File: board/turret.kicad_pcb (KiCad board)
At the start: 2 copper layers, 29 parts, among them M1 SRV_LAS, M2 SRV_SEN, U1 STM32F103CBTx, U2 W25Q32JVSS, U3 TPA2005D1DGN

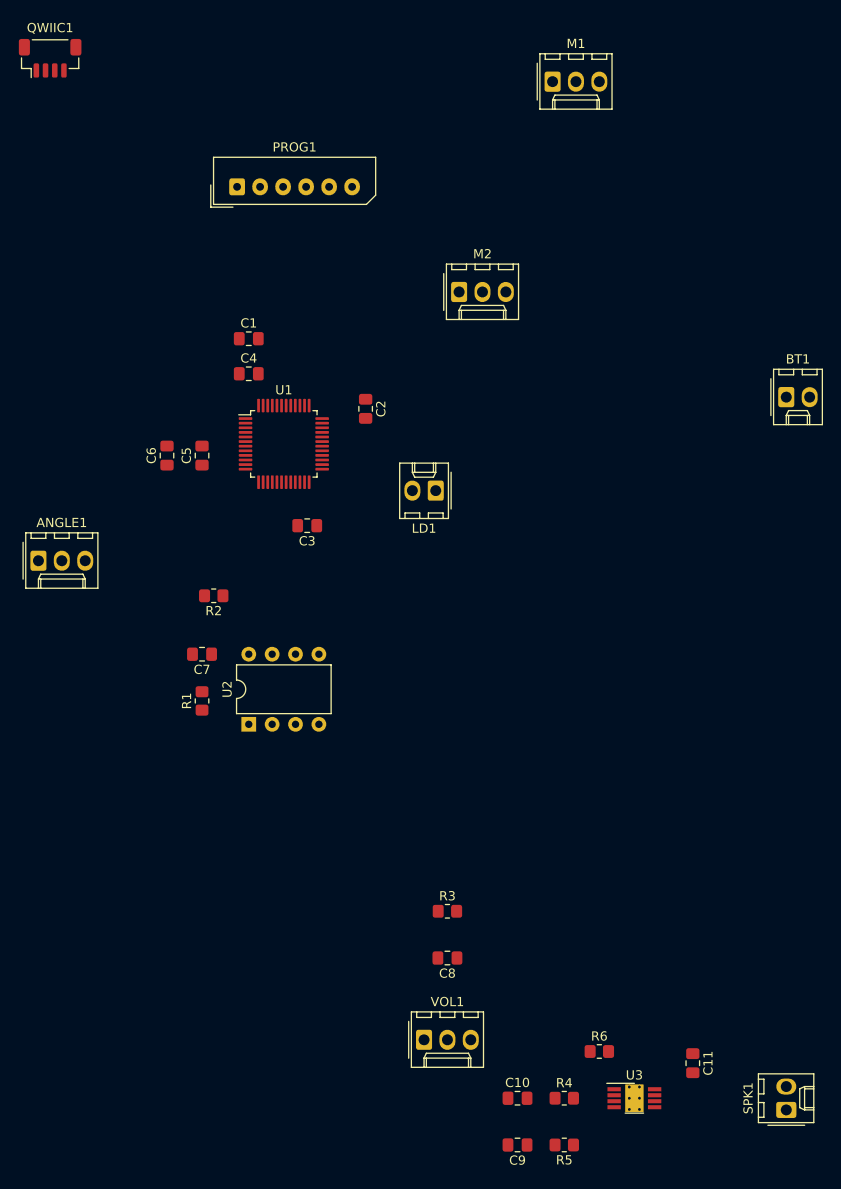
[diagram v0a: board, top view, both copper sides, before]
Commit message: Partially route board
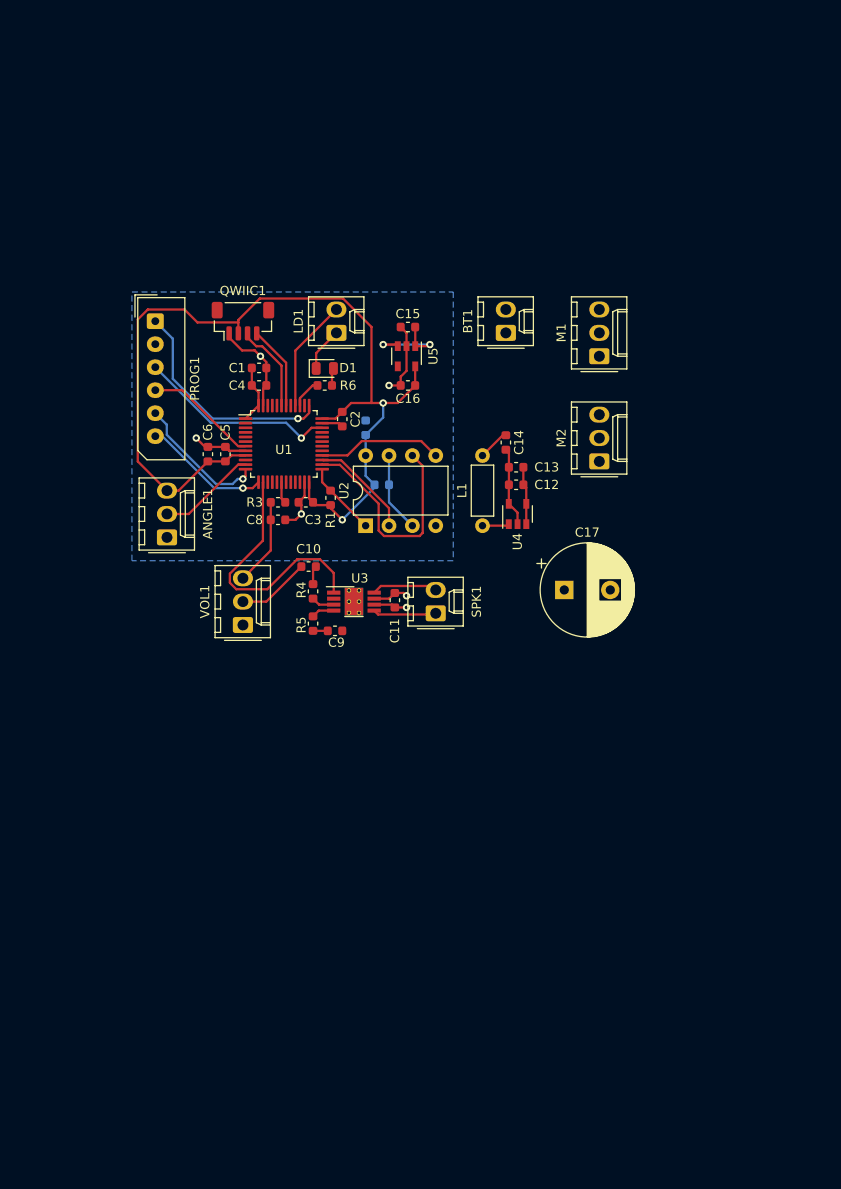
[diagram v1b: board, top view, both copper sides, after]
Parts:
- added C12: 22u, Capacitor_SMD:C_0603_1608Metric, F.Cu at (91.3, 69.2)
- added C13: 22u, Capacitor_SMD:C_0603_1608Metric, F.Cu at (91.3, 67.3)
- added C14: 4u7, Capacitor_SMD:C_0603_1608Metric, F.Cu at (90.2, 64.6)
- added C15: 100n, Capacitor_SMD:C_0603_1608Metric, F.Cu at (79.5, 52.1)
- added C16: 100n, Capacitor_SMD:C_0603_1608Metric, F.Cu at (79.5, 58.4)
- added C17: 1000u, Capacitor_THT:CP_Radial_D10.0mm_P5.00mm, F.Cu at (96.5, 80.6)
- added D1: LED, LED_SMD:LED_0805_2012Metric, F.Cu at (70.5, 56.6)
- added L1: 2u2, Inductor_THT:L_Axial_L5.3mm_D2.2mm_P7.62mm_Horizontal_Vishay_IM-1, F.Cu at (87.6, 73.7)
- added U4: TPS61322xADBV, Package_TO_SOT_SMD:SOT-23-5, F.Cu at (91.4, 72.4)
- added U5: TLV70028_SOT23-5, Package_TO_SOT_SMD:SOT-23-5, F.Cu at (79.4, 55.2)
- C1, C10, C11, C2, C3, C4, C5, C6, C8, C9: footprint Capacitor_SMD:C_0805_2012Metric_Pad1.18x1.45mm_HandSolder -> Capacitor_SMD:C_0603_1608Metric
- C7: footprint Capacitor_SMD:C_0805_2012Metric_Pad1.18x1.45mm_HandSolder -> Capacitor_SMD:C_0603_1608Metric; moved to B.Cu
- R1, R4, R5: footprint Resistor_SMD:R_0805_2012Metric_Pad1.20x1.40mm_HandSolder -> Resistor_SMD:R_0603_1608Metric
- R2: footprint Resistor_SMD:R_0805_2012Metric_Pad1.20x1.40mm_HandSolder -> Resistor_SMD:R_0603_1608Metric; moved to B.Cu
- R3: value 400 -> 200; footprint Resistor_SMD:R_0805_2012Metric_Pad1.20x1.40mm_HandSolder -> Resistor_SMD:R_0603_1608Metric
- R6: value 50K -> 100; footprint Resistor_SMD:R_0805_2012Metric_Pad1.20x1.40mm_HandSolder -> Resistor_SMD:R_0603_1608Metric
- moved R6 78.3 mm to (70.5, 58.4), turned to 180 degrees
- moved SPK1 66.1 mm to (82.5, 83.2)
- moved R5 62.9 mm to (69.2, 84.3), turned to 270 degrees
- moved C10 62.1 mm to (68.7, 78.1)
- moved U3 62.0 mm to (73.7, 81.9)
- moved R4 61.5 mm to (69.2, 80.8), turned to 270 degrees
- moved C11 59.8 mm to (78.1, 81.8)
- moved C9 59.3 mm to (71.6, 85.1), turned to 0 degrees
- moved C8 51.1 mm to (65.4, 73.0), turned to 0 degrees
- moved VOL1 49.2 mm to (61.6, 84.5), turned to 90 degrees
- moved R3 48.1 mm to (65.4, 71.1), turned to 180 degrees
- moved QWIIC1 35.4 mm to (61.6, 51.4)
- moved BT1 31.3 mm to (90.2, 52.7), turned to 90 degrees
- moved C7 30.4 mm to (74.9, 63.0), turned to 90 degrees
- moved M1 30.3 mm to (100.3, 55.2), turned to 90 degrees
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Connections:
- ANGLE1 pad 3: +3V3 -> VDD
- BT1 pad 1: +3V3 -> Net-(BT1-Pad1)
- BT1 pad 2: (no net) -> GNDA
- C1 pad 1: +3V3 -> VDD
- C11 pad 2: +3V3 -> +5V
- C2 pad 1: +3V3 -> VDD
- C3 pad 1: +3V3 -> VDD
- C4 pad 1: +3V3 -> VDD
- C5 pad 1: +3V3 -> VDD
- C6 pad 1: +3V3 -> VDD
- C7 pad 1: +3V3 -> VDD
- M1 pad 2: +3V3 -> +5V
- M2 pad 2: +3V3 -> +5V
- QWIIC1 pad 2: +3V3 -> VDD
- R1 pad 2: +3V3 -> VDD
- R2 pad 2: +3V3 -> VDD
- R6 pad 1: /MUTE -> Net-(D1-Pad2)
- R6 pad 2: Net-(R6-Pad2) -> /TGT_LED
- U1 pad 1: +3V3 -> VDD
- U1 pad 10: (no net) -> Net-(U1-Pad10)
- U1 pad 14: /SPI_NSS -> /AU_ENAB
- U1 pad 15: /SPI_SCK -> Net-(U1-Pad15)
- U1 pad 16: /SPI_MISO -> Net-(U1-Pad16)
- U1 pad 17: /SPI_MOSI -> Net-(U1-Pad17)
- U1 pad 18: (no net) -> /AUDIO
- U1 pad 19: (no net) -> Net-(U1-Pad19)
- U1 pad 2: (no net) -> Net-(U1-Pad2)
- U1 pad 20: (no net) -> Net-(U1-Pad20)
- U1 pad 21: (no net) -> Net-(U1-Pad21)
- U1 pad 22: (no net) -> Net-(U1-Pad22)
- U1 pad 24: +3V3 -> VDD
- U1 pad 25: (no net) -> /SPI_NSS
- U1 pad 26: (no net) -> /SPI_SCK
- U1 pad 27: /LASER -> /SPI_MISO
- U1 pad 28: (no net) -> /SPI_MOSI
- U1 pad 29: /AUDIO -> /SRV_SEN
- U1 pad 3: (no net) -> Net-(U1-Pad3)
- U1 pad 30: /MUTE -> /SRV_LAS
- U1 pad 31: (no net) -> Net-(U1-Pad31)
- U1 pad 32: (no net) -> Net-(U1-Pad32)
- U1 pad 33: (no net) -> Net-(U1-Pad33)
- U1 pad 36: +3V3 -> VDD
- U1 pad 38: (no net) -> Net-(U1-Pad38)
- U1 pad 39: (no net) -> /TGT_LED
- U1 pad 4: (no net) -> Net-(U1-Pad4)
- U1 pad 40: /SRV_SEN -> /LASER
- U1 pad 41: /SRV_LAS -> Net-(U1-Pad41)
- U1 pad 44: (no net) -> Net-(U1-Pad44)
- U1 pad 45: (no net) -> Net-(U1-Pad45)
- U1 pad 46: (no net) -> Net-(U1-Pad46)
- U1 pad 48: +3V3 -> VDD
- U1 pad 5: (no net) -> Net-(U1-Pad5)
- U1 pad 6: (no net) -> Net-(U1-Pad6)
- U1 pad 9: +3V3 -> VDD
- U2 pad 8: +3V3 -> VDD
- U3 pad 1: Net-(R6-Pad2) -> /AU_ENAB
- U3 pad 6: +3V3 -> +5V
- U3 pad 9: (no net) -> GNDA
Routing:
- net VDD: track 0.00 -> 110.4 mm, vias 0 -> 2
- net GNDA: track 0.00 -> 50.0 mm, vias 0 -> 5
- net /AU_ENAB: track 0.00 -> 28.1 mm
- net /SPI_SCK: track 0.00 -> 24.9 mm
- net /SWCLK: track 0.00 -> 24.7 mm, vias 0 -> 1
- net /SWDIO: track 0.00 -> 21.8 mm, vias 0 -> 1
- net /SER_TX: track 0.00 -> 14.8 mm, vias 0 -> 1
- net Net-(BT1-Pad1): track 0.00 -> 13.9 mm, vias 0 -> 2
- net /SER_RX: track 0.00 -> 13.8 mm, vias 0 -> 1
- net /SPI_MOSI: track 0.00 -> 13.6 mm
- net /RESET: track 0.00 -> 12.3 mm
- net /LASER: track 0.00 -> 12.3 mm
- net /SPI_MISO: track 0.00 -> 11.3 mm
- net /ANGLE_POT: track 0.00 -> 10.8 mm
- net +5V: track 0.00 -> 9.95 mm, vias 0 -> 1
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- added copper zone on B.Cu, net GNDA

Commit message: Route PCB
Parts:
- added C18: 100p, Capacitor_SMD:C_0603_1608Metric, F.Cu at (91.9, 77.5)
- added C19: 20p, Capacitor_SMD:C_0603_1608Metric, F.Cu at (91.9, 79.4)
- added D2: D_Schottky, Diode_SMD:D_SMA, F.Cu at (90.1, 74.9)
- added Q1: BC547, Package_TO_SOT_THT:TO-92_Inline_Wide, F.Cu at (97.2, 82.5)
- added R7: 5, Resistor_SMD:R_0603_1608Metric, F.Cu at (88.5, 77.5)
- added R8: 1K, Resistor_SMD:R_0603_1608Metric, F.Cu at (87.4, 82.5)
- L1: footprint Inductor_THT:L_Axial_L5.3mm_D2.2mm_P7.62mm_Horizontal_Vishay_IM-1 -> Inductor_THT:L_Axial_L7.0mm_D3.3mm_P10.16mm_Horizontal_Fastron_MICC
- R6: value 100 -> 50
- moved LD1 40.5 mm to (102.2, 79.4)
- moved C17 24.7 mm to (91.4, 56.5), turned to 90 degrees
- moved M1 17.3 mm to (102.2, 72.4)
- moved BT1 12.1 mm to (102.2, 53.3)
- moved C9 10.3 mm to (61.4, 83.2), turned to 180 degrees
- moved VOL1 9.86 mm to (52.1, 81.9), turned to 0 degrees
- moved C10 7.72 mm to (61.4, 80.6)
- moved R2 5.17 mm to (77.6, 64.1)
- moved R5 4.73 mm to (64.6, 83.2), turned to 180 degrees
- moved R4 4.60 mm to (64.6, 80.6), turned to 0 degrees
- moved M2 4.26 mm to (102.2, 62.9)
- moved C11 3.81 mm to (74.3, 81.8)
- moved SPK1 3.81 mm to (78.7, 83.2)
- moved U3 3.81 mm to (69.8, 81.9)
- moved C12 2.29 mm to (92.6, 67.3)
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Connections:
- C17 pad 1: +5V -> Net-(BT1-Pad1)
- LD1 pad 1: GNDA -> Net-(LD1-Pad1)
- LD1 pad 2: /LASER -> +5V
- U1 pad 15: Net-(U1-Pad15) -> /LASER
- U1 pad 40: /LASER -> Net-(U1-Pad40)
- U3 pad 2: (no net) -> Net-(U3-Pad2)
- U5 pad 4: Net-(U5-Pad4) -> GNDA
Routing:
- net /SRV_LAS: track 0.00 -> 69.0 mm
- net +5V: track 9.95 -> 78.8 mm, vias 1 -> 2
- net /SRV_SEN: track 0.00 -> 58.6 mm
- net GNDA: track 50.0 -> 103.0 mm, vias 5 -> 14
- net Net-(BT1-Pad1): track 13.9 -> 42.3 mm, vias 2 -> 3
- net VDD: track 110.4 -> 89.2 mm
- net /LASER: track 12.3 -> 32.6 mm
- net /AU_ENAB: track 28.1 -> 14.2 mm
- net Net-(Q1-Pad2): track 0.00 -> 7.24 mm
- net Net-(D2-Pad2): track 2.93 -> 9.54 mm
- net Net-(LD1-Pad1): track 0.00 -> 6.40 mm
- net Net-(C8-Pad1): track 9.51 -> 15.9 mm, vias 0 -> 2
- net Net-(C18-Pad1): track 0.00 -> 3.78 mm
- net /RESET: track 12.3 -> 15.5 mm, vias 0 -> 1
- net Net-(R2-Pad1): track 8.67 -> 11.0 mm
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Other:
- board outline added: 57.1 x 38.7 mm
- net class PWR added: clearance 0.2, trace_width 0.4, via_dia 0.8, via_drill 0.4
